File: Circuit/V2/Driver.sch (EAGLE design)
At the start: 36 parts

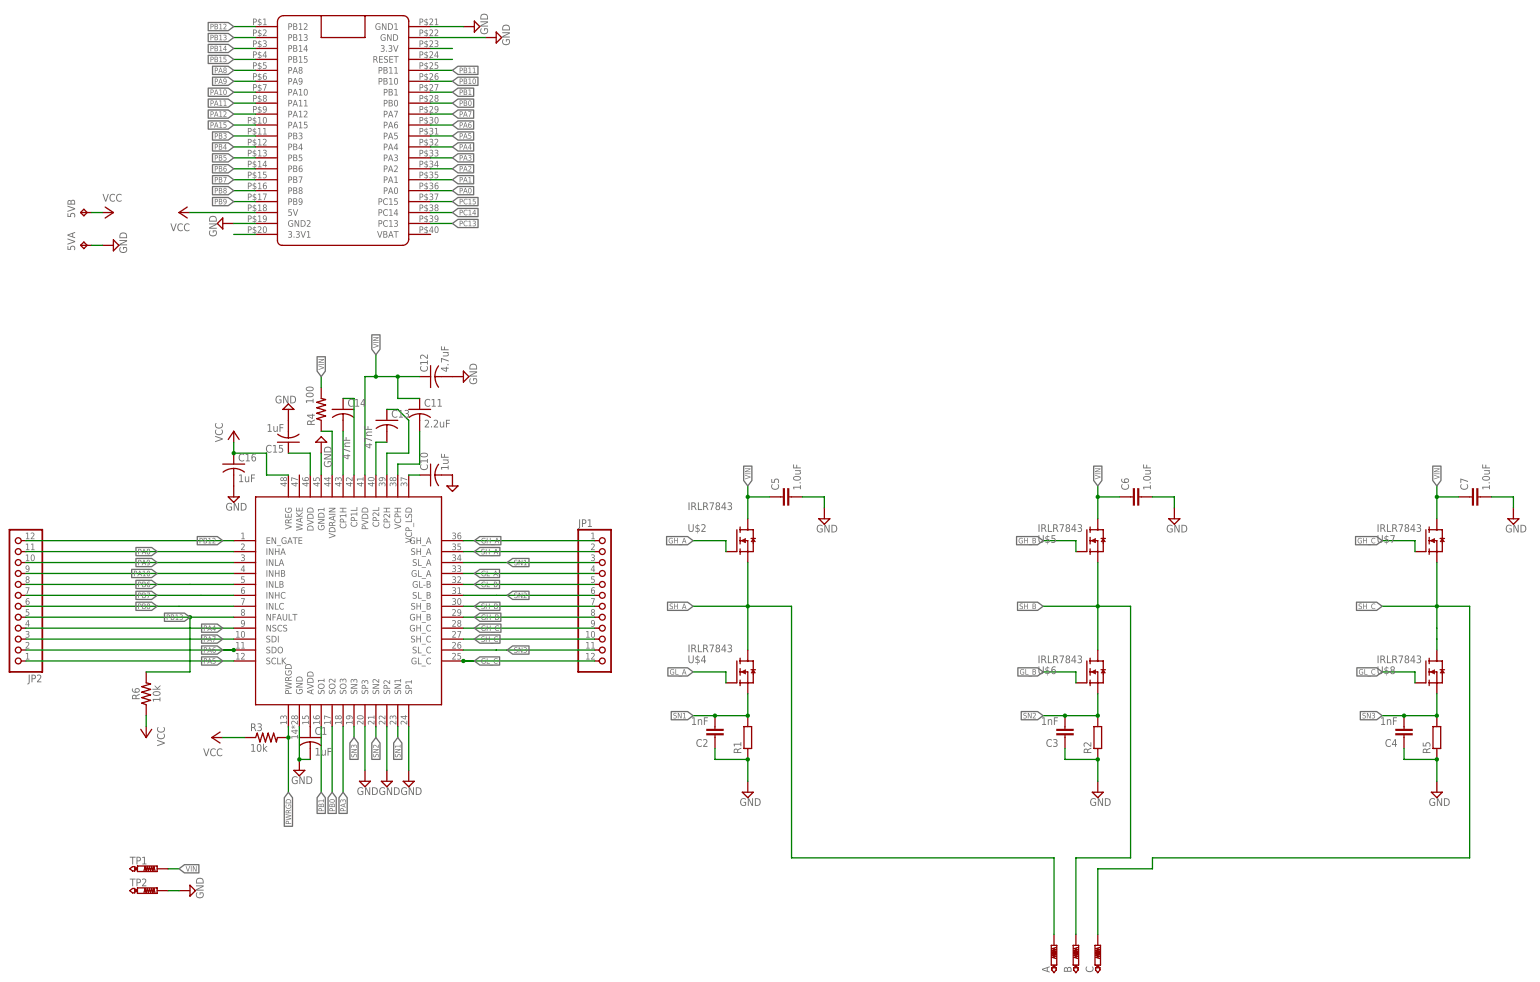
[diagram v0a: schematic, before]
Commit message: Designed and auto routed BLDC driver V2 circuit
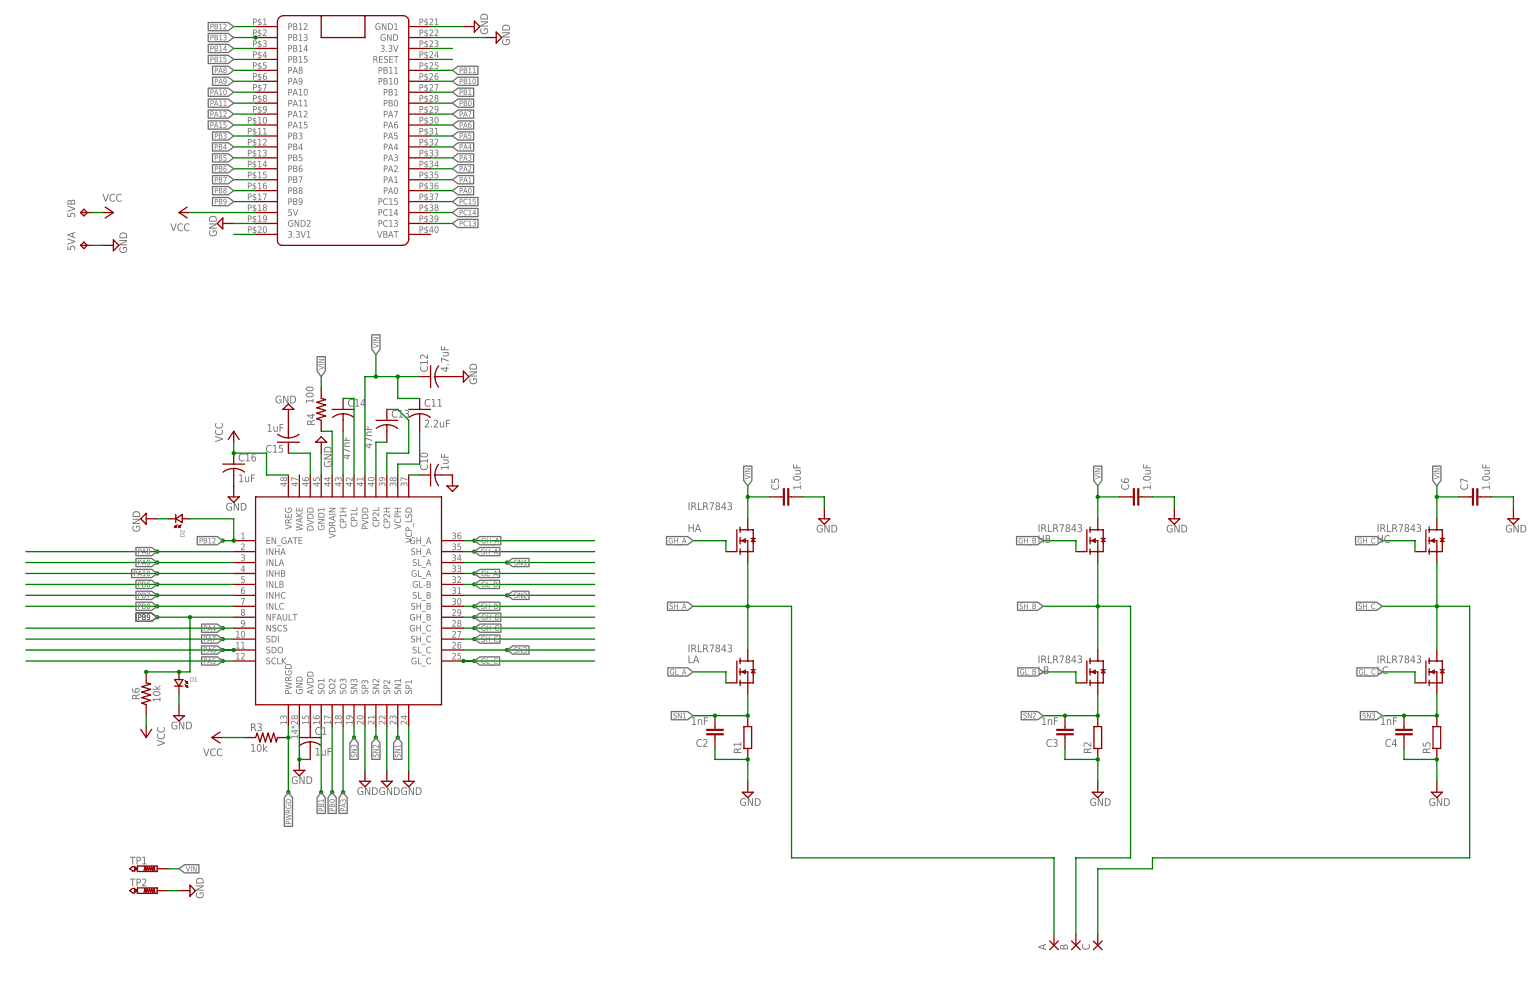
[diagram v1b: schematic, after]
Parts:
- removed JP1, JP2: (no value), pinhead:PINHD-1X12
- added D1, D2: (no value), standardparts:LED.0805
- A, B, C: value PTR1PAD1-20Y -> (none); device testpad:PTR1PAD1-20Y -> wirepad:SMD5
- renumbered U$2 to HA, U$4 to LA, U$5 to HB, U$6 to LB, U$7 to HC, U$8 to LC
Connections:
- net GH_A: no longer JP1.1
- net GH_B: no longer JP1.8
- net GH_C: no longer JP1.9
- net GL_A: no longer JP1.4
- net GL_B: no longer JP1.5
- net GL_C: no longer JP1.12
- net GND: now also D1.2, D2.2
- net PA10: no longer JP2.9
- net PA4: no longer JP2.4
- net PA5: no longer JP2.1
- net PA6: no longer JP2.2
- net PA7: no longer JP2.3
- net PA8: no longer JP2.11
- net PA9: no longer JP2.10
- net PB12: now also D2.1; no longer JP2.12
- net PB13: no longer JP2.5, R6.2, U$3.NFAULT
- net PB6: no longer JP2.8
- net PB7: no longer JP2.7
- net PB8: no longer JP2.6
- net PB9: now also D1.1, R6.2, U$3.NFAULT
- net SH_A: now also A.P; no longer A.TP, JP1.2
- net SH_B: now also B.P; no longer B.TP, JP1.7
- net SH_C: now also C.P; no longer C.TP, JP1.10
- net SN1: no longer JP1.3
- net SN2: no longer JP1.6
- net SN3: no longer JP1.11

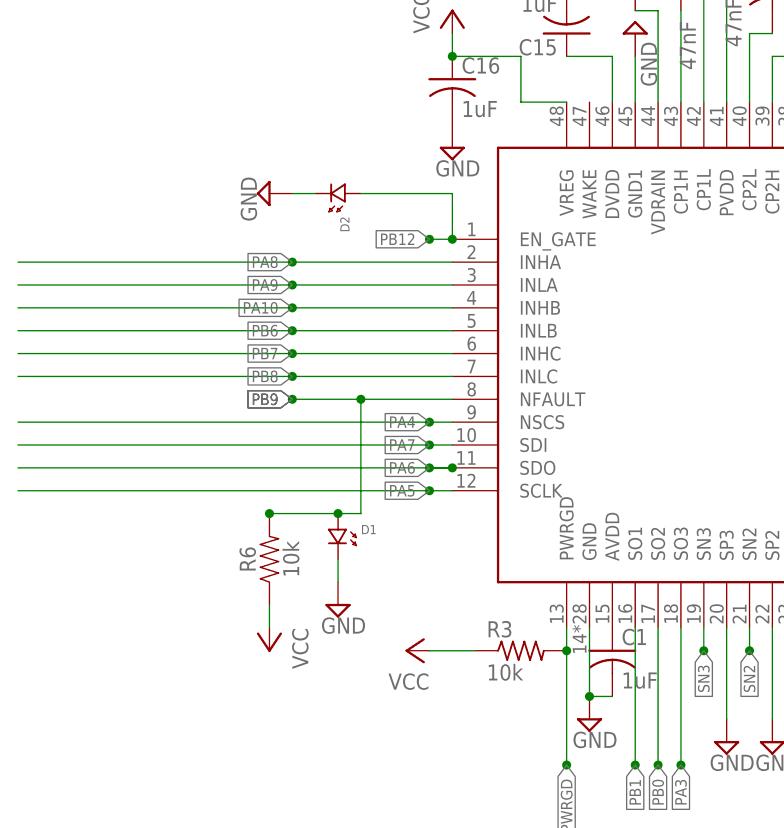
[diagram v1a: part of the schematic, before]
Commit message: Delete some resistors and capacitors value in Tvalue and Bvalue layers
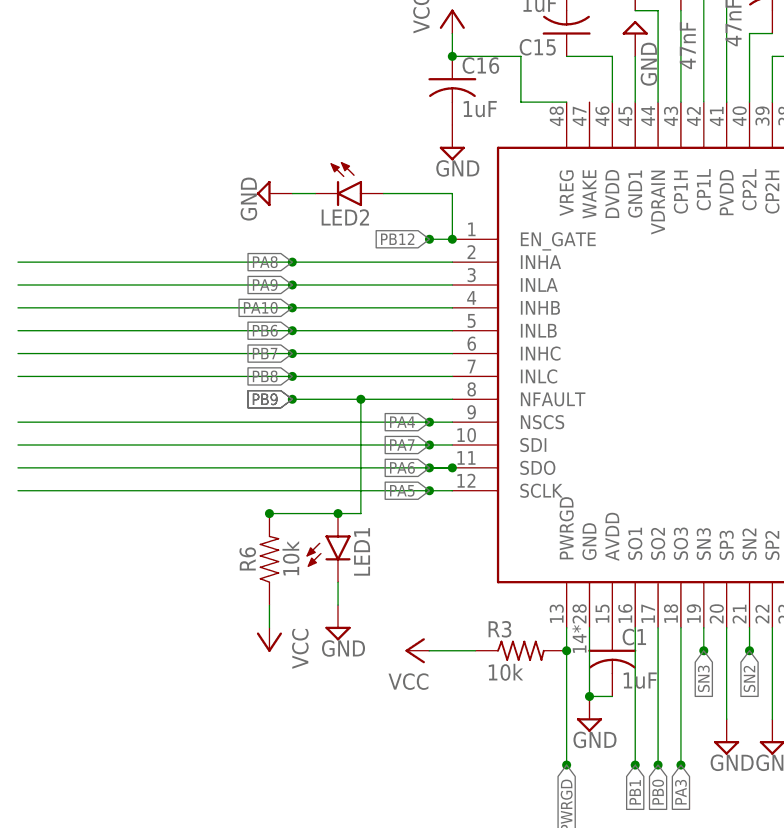
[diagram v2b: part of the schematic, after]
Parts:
- removed D1, D2: (no value), standardparts:LED.0805
- added LED1, LED2: (no value), led:LEDCHIPLED_0805
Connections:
- net GND: now also LED1.C, LED2.C; no longer D1.2, D2.2
- net PB12: now also LED2.A; no longer D2.1
- net PB9: now also LED1.A; no longer D1.1
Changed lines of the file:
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@@
 <part name="P+5" library="supply1" library_urn="urn:adsk.eagle:library:371" deviceset="VCC" device=""/>
 <part name="SUPPLY20" library="supply2" library_urn="urn:adsk.eagle:library:372" deviceset="GND" device=""/>
-<part name="D1" library="standardparts" deviceset="LED" device=".0805"/>
 <part name="SUPPLY21" library="supply2" library_urn="urn:adsk.eagle:library:372" deviceset="GND" device=""/>
-<part name="D2" library="standardparts" deviceset="LED" device=".0805"/>
 <part name="SUPPLY22" library="supply2" library_urn="urn:adsk.eagle:library:372" deviceset="GND" device=""/>
 <part name="A" library="wirepad" library_urn="urn:adsk.eagle:library:412" deviceset="SMD5" device="" package3d_urn="urn:adsk.eagle:package:30841/1"/>
 <part name="B" library="wirepad" library_urn="urn:adsk.eagle:library:412" deviceset="SMD5" device="" package3d_urn="urn:adsk.eagle:package:30841/1"/>
 <part name="C" library="wirepad" library_urn="urn:adsk.eagle:library:412" deviceset="SMD5" device="" package3d_urn="urn:adsk.eagle:package:30841/1"/>
+<part name="LED1" library="led" library_urn="urn:adsk.eagle:library:259" deviceset="LED" device="CHIPLED_0805" package3d_urn="urn:adsk.eagle:package:15821/2"/>
+<part name="LED2" library="led" library_urn="urn:adsk.eagle:library:259" deviceset="LED" device="CHIPLED_0805" package3d_urn="urn:adsk.eagle:package:15821/2"/>
 </parts>
 <sheets>
@@
 <attribute name="VALUE" x="8.255" y="76.835" size="1.778" layer="96" rot="R90"/>
 </instance>
-<instance part="D1" gate="G$1" x="20.32" y="-22.86" smashed="yes" rot="R270">
-<attribute name="NAME" x="22.86" y="-21.59" size="1.016" layer="95" rot="MR180"/>
-<attribute name="VALUE" x="22.86" y="-24.13" size="1.016" layer="96"/>
-</instance>
-<instance part="SUPPLY21" gate="GND" x="20.32" y="-30.48" smashed="yes">
-<attribute name="VALUE" x="18.415" y="-33.655" size="1.778" layer="96"/>
-</instance>
-<instance part="D2" gate="G$1" x="20.32" y="15.24" smashed="yes" rot="R180">
-<attribute name="NAME" x="21.59" y="12.7" size="1.016" layer="95" rot="MR270"/>
-<attribute name="VALUE" x="19.05" y="12.7" size="1.016" layer="96" rot="R270"/>
+<instance part="SUPPLY21" gate="GND" x="20.32" y="-33.02" smashed="yes">
+<attribute name="VALUE" x="18.415" y="-36.195" size="1.778" layer="96"/>
 </instance>
 <instance part="SUPPLY22" gate="GND" x="12.7" y="15.24" smashed="yes" rot="R270">
@@
 <attribute name="NAME" x="231.8258" y="-84.963" size="1.778" layer="95" rot="R90"/>
 <attribute name="VALUE" x="236.982" y="-84.963" size="1.778" layer="96" rot="R90"/>
+</instance>
+<instance part="LED1" gate="G$1" x="20.32" y="-22.86" smashed="yes">
+<attribute name="NAME" x="23.876" y="-27.432" size="1.778" layer="95" rot="R90"/>
+<attribute name="VALUE" x="26.035" y="-27.432" size="1.778" layer="96" rot="R90"/>
+</instance>
+<instance part="LED2" gate="G$1" x="22.86" y="15.24" smashed="yes" rot="R270">
+<attribute name="NAME" x="18.288" y="11.684" size="1.778" layer="95"/>
+<attribute name="VALUE" x="18.288" y="9.525" size="1.778" layer="96"/>
 </instance>
 </instances>
@@
 </segment>
 <segment>
-<pinref part="D1" gate="G$1" pin="2"/>
-<pinref part="SUPPLY21" gate="GND" pin="GND"/>
-<wire x1="20.32" y1="-27.94" x2="20.32" y2="-25.4" width="0.1524" layer="91"/>
-</segment>
-<segment>
-<pinref part="D2" gate="G$1" pin="2"/>
 <wire x1="17.78" y1="15.24" x2="15.24" y2="15.24" width="0.1524" layer="91"/>
 <pinref part="SUPPLY22" gate="GND" pin="GND"/>
+<pinref part="LED2" gate="G$1" pin="C"/>
+</segment>
+<segment>
+<pinref part="LED1" gate="G$1" pin="C"/>
+<pinref part="SUPPLY21" gate="GND" pin="GND"/>
+<wire x1="20.32" y1="-27.94" x2="20.32" y2="-30.48" width="0.1524" layer="91"/>
 </segment>
 </net>
@@
 <label x="30.48" y="10.16" size="1.27" layer="95" rot="R180" xref="yes"/>
 <wire x1="33.02" y1="10.16" x2="33.02" y2="15.24" width="0.1524" layer="91"/>
-<wire x1="33.02" y1="15.24" x2="22.86" y2="15.24" width="0.1524" layer="91"/>
-<pinref part="D2" gate="G$1" pin="1"/>
+<wire x1="33.02" y1="15.24" x2="25.4" y2="15.24" width="0.1524" layer="91"/>
 <wire x1="33.02" y1="10.16" x2="30.48" y2="10.16" width="0.1524" layer="91"/>
 <junction x="30.48" y="10.16"/>
 <junction x="33.02" y="10.16"/>
+<pinref part="LED2" gate="G$1" pin="A"/>
 </segment>
 </net>
@@
 <wire x1="22.86" y1="-7.62" x2="22.86" y2="-20.32" width="0.1524" layer="91"/>
 <wire x1="22.86" y1="-20.32" x2="20.32" y2="-20.32" width="0.1524" layer="91"/>
-<pinref part="D1" gate="G$1" pin="1"/>
+<pinref part="U$3" gate="G$1" pin="NFAULT"/>
 <wire x1="20.32" y1="-20.32" x2="12.7" y2="-20.32" width="0.1524" layer="91"/>
-<junction x="20.32" y="-20.32"/>
-<pinref part="U$3" gate="G$1" pin="NFAULT"/>
 <wire x1="33.02" y1="-7.62" x2="22.86" y2="-7.62" width="0.1524" layer="91"/>
 <label x="15.24" y="-7.62" size="1.27" layer="95" rot="R180" xref="yes"/>
@@
 <wire x1="22.86" y1="-7.62" x2="15.24" y2="-7.62" width="0.1524" layer="91"/>
 <junction x="12.7" y="-20.32"/>
-</segment>
-</net>
+<pinref part="LED1" gate="G$1" pin="A"/>
+<junction x="20.32" y="-20.32"/>
+</segment>
+</net>
